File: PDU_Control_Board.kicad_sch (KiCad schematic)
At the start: 203 parts, among them J1 Current_Sensor, J10 Precharge_2, J11 Shunt_2, J12 VIN_Enable, J13 1-776087-1, J2 Shunt_1, J20 VDC_OUT2, J21 VDC_OUT1, J22 VDC_IN, J3 SWD, J4 Precharge_1, J5 Precharge_2, J6 Shunt_2, J7 VIN_Enable, J8 Precharge_1, J9 Shunt_1, Q1 BSP75N, Q10 BC817, Q2 BSP75N, Q3 BSP75N, Q4 BSP75N, Q5 BSP75N, Q6 BC817, Q7 BC817, Q8 BC817, Q9 BC817, U1 LMV321, U2 APM32F405xG, U3 LMV321, U4 LMV321, U5 LMV321, U6 LMV321, Y2 X322516MOB4SI

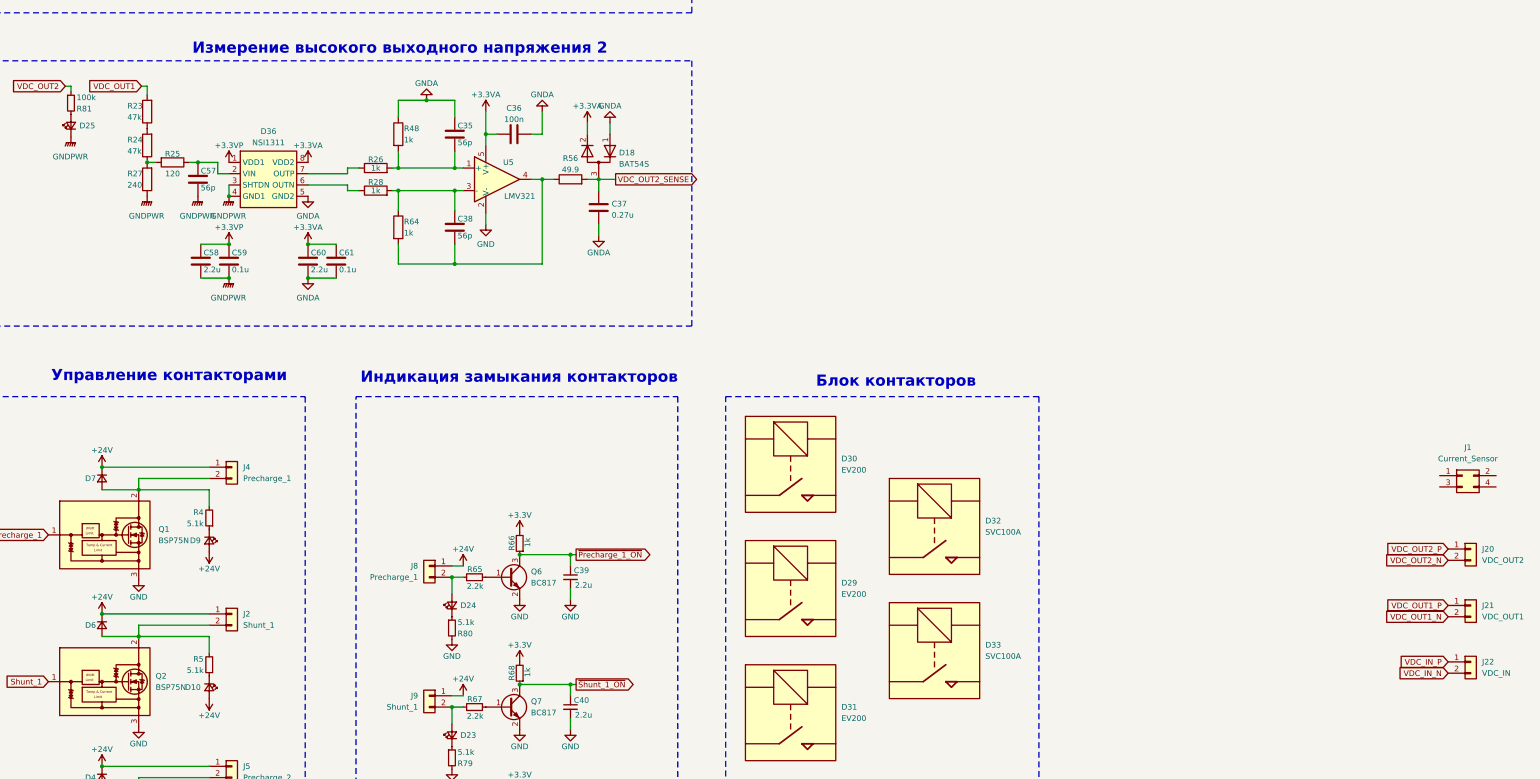
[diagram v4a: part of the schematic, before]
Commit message: VER1.0: обрезал плату
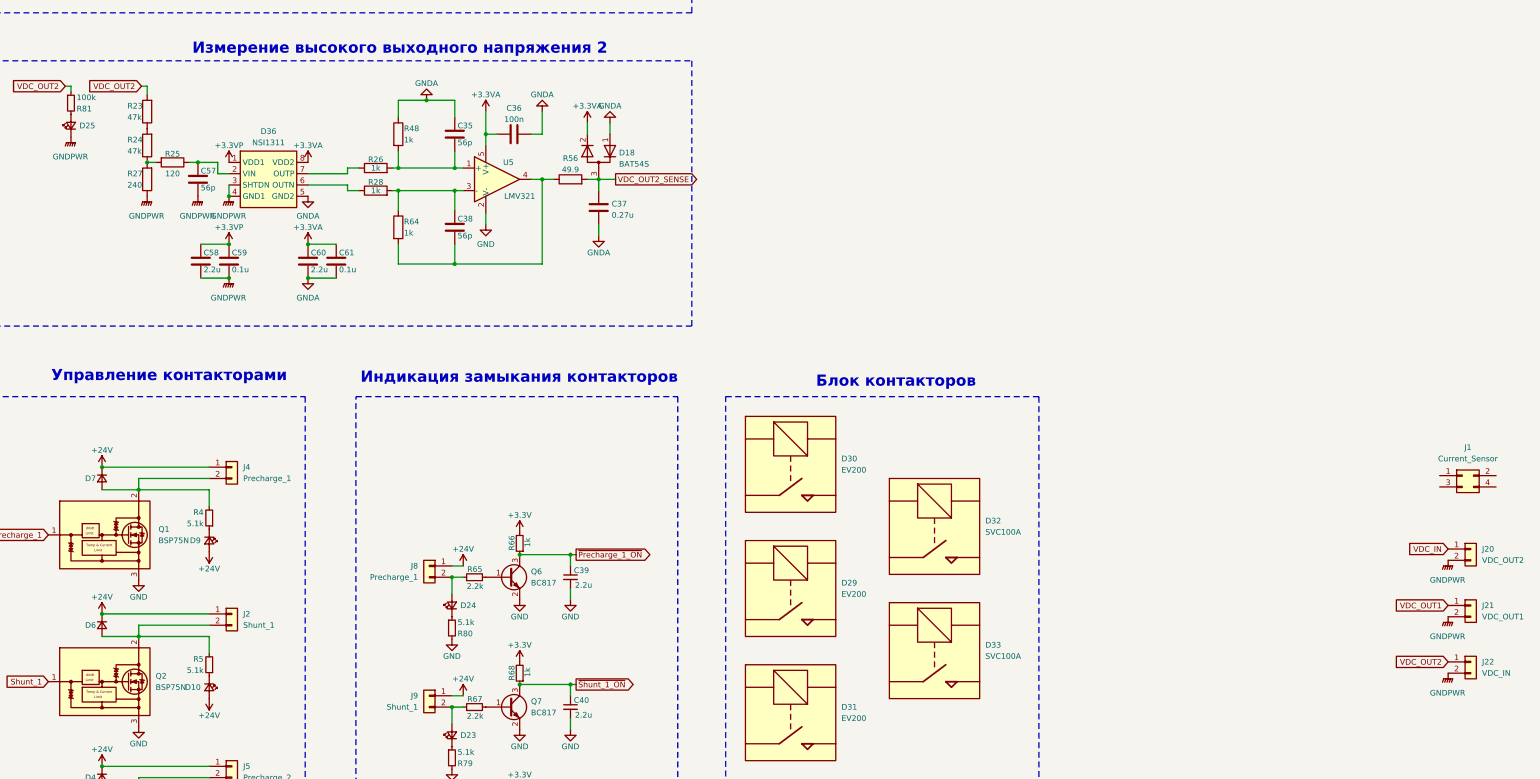
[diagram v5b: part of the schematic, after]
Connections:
- net VDC_IN_N is gone; now on net GNDPWR: J22.2 (Pin_2)
- net VDC_IN_P is gone; now on net VDC_OUT2: J22.1 (Pin_1)
- net VDC_OUT1_N is gone; now on net GNDPWR: J21.2 (Pin_2)
- net VDC_OUT2_N is gone; now on net GNDPWR: J20.2 (Pin_2)
- net VDC_OUT2_P is gone; now on net VDC_IN: J20.1 (Pin_1)
- net VDC_OUT1: now also J21.1 (Pin_1); no longer R23.2
- net VDC_OUT1_P: no longer J21.1 (Pin_1)
- net VDC_OUT2: now also R23.2
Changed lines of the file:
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@@
 		)
 	)
-	(global_label "VDC_OUT1_P"
+	(global_label "VDC_IN"
 		(shape input)
-		(at 946.15 527.05 180)
+		(at 946.15 514.35 180)
 		(fields_autoplaced yes)
 		(effects
@@
 		)
 		(property "Intersheetrefs" "${INTERSHEET_REFS}"
-			(at 933.3433 527.05 0)
+			(at 937.7939 514.35 0)
 			(effects
 				(font
@@
 		)
 	)
-	(global_label "~{Precharge_1_ON}"
+	(global_label "VDC_OUT1"
 		(shape input)
-		(at 307.34 323.85 0)
+		(at 946.15 527.05 180)
 		(fields_autoplaced yes)
 		(effects
@@
 				(size 1.27 1.27)
 			)
-			(justify left)
+			(justify right)
 		)
 		(property "Intersheetrefs" "${INTERSHEET_REFS}"
-			(at 325.6861 323.85 0)
+			(at 935.5047 527.05 0)
 			(effects
 				(font
 					(size 1.27 1.27)
 				)
-				(justify left)
+				(justify right)
 				(hide yes)
 			)
 		)
 	)
-	(global_label "VDC_IN_SENSE"
+	(global_label "~{Precharge_1_ON}"
 		(shape input)
-		(at 307.34 400.05 0)
+		(at 307.34 323.85 0)
 		(fields_autoplaced yes)
 		(effects
@@
 		)
 		(property "Intersheetrefs" "${INTERSHEET_REFS}"
-			(at 323.8718 400.05 0)
+			(at 325.6861 323.85 0)
 			(effects
 				(font
@@
 		)
 	)
-	(global_label "Current"
+	(global_label "VDC_IN_SENSE"
 		(shape input)
-		(at 797.56 295.91 180)
+		(at 307.34 400.05 0)
 		(fields_autoplaced yes)
 		(effects
@@
 				(size 1.27 1.27)
 			)
-			(justify right)
+			(justify left)
 		)
 		(property "Intersheetrefs" "${INTERSHEET_REFS}"
-			(at 787.6201 295.91 0)
+			(at 323.8718 400.05 0)
 			(effects
 				(font
 					(size 1.27 1.27)
 				)
-				(justify right)
+				(justify left)
 				(hide yes)
 			)
 		)
 	)
-	(global_label "VDC_OUT2_P"
+	(global_label "Current"
 		(shape input)
-		(at 946.15 514.35 180)
+		(at 797.56 295.91 180)
 		(fields_autoplaced yes)
 		(effects
@@
 		)
 		(property "Intersheetrefs" "${INTERSHEET_REFS}"
-			(at 933.089 514.35 0)
+			(at 787.6201 295.91 0)
 			(effects
 				(font
@@
 		)
 	)
-	(global_label "VDC_OUT1_N"
-		(shape input)
-		(at 946.15 529.59 180)
-		(fields_autoplaced yes)
-		(effects
-			(font
-				(size 1.27 1.27)
-			)
-			(justify right)
-		)
-		(property "Intersheetrefs" "${INTERSHEET_REFS}"
-			(at 933.3433 529.59 0)
-			(effects
-				(font
-					(size 1.27 1.27)
-				)
-				(justify right)
-				(hide yes)
-			)
-		)
-	)
 	(global_label "Shunt_1"
 		(shape input)
@@
 		)
 	)
-	(global_label "VDC_IN_P"
-		(shape input)
-		(at 946.15 539.75 180)
-		(fields_autoplaced yes)
-		(effects
-			(font
-				(size 1.27 1.27)
-			)
-			(justify right)
-		)
-		(property "Intersheetrefs" "${INTERSHEET_REFS}"
-			(at 935.6325 539.75 0)
-			(effects
-				(font
-					(size 1.27 1.27)
-				)
-				(justify right)
-				(hide yes)
-			)
-		)
-	)
-	(global_label "VDC_OUT1"
+	(global_label "VDC_OUT2"
 		(shape input)
 		(at 652.145 410.21 180)
@@
 		)
 		(property "Intersheetrefs" "${INTERSHEET_REFS}"
-			(at 641.4997 410.21 0)
+			(at 639.7255 410.21 0)
 			(effects
 				(font
@@
 		)
 	)
-	(global_label "CAN1_RXD_MCU"
-		(shape bidirectional)
-		(at 307.34 331.47 0)
+	(global_label "VDC_OUT2"
+		(shape input)
+		(at 946.15 539.75 180)
 		(fields_autoplaced yes)
 		(effects
@@
 				(size 1.27 1.27)
 			)
-			(justify left)
+			(justify right)
 		)
 		(property "Intersheetrefs" "${INTERSHEET_REFS}"
-			(at 325.9923 331.47 0)
+			(at 933.7305 539.75 0)
 			(effects
 				(font
 					(size 1.27 1.27)
 				)
-				(justify left)
+				(justify right)
 				(hide yes)
 			)
 		)
 	)
-	(global_label "VDC_IN_N"
-		(shape input)
-		(at 946.15 542.29 180)
+	(global_label "CAN1_RXD_MCU"
+		(shape bidirectional)
+		(at 307.34 331.47 0)
 		(fields_autoplaced yes)
 		(effects
@@
 				(size 1.27 1.27)
 			)
-			(justify right)
+			(justify left)
 		)
 		(property "Intersheetrefs" "${INTERSHEET_REFS}"
-			(at 935.6325 542.29 0)
+			(at 325.9923 331.47 0)
 			(effects
 				(font
 					(size 1.27 1.27)
 				)
-				(justify right)
+				(justify left)
 				(hide yes)
 			)
@@
 		)
 	)
-	(global_label "VDC_OUT2_N"
-		(shape input)
-		(at 946.15 516.89 180)
-		(fields_autoplaced yes)
-		(effects
-			(font
-				(size 1.27 1.27)
-			)
-			(justify right)
-		)
-		(property "Intersheetrefs" "${INTERSHEET_REFS}"
-			(at 933.089 516.89 0)
-			(effects
-				(font
-					(size 1.27 1.27)
-				)
-				(justify right)
-				(hide yes)
-			)
-		)
-	)
 	(symbol
 		(lib_id "power:GNDA")
@@
 	)
 	(symbol
+		(lib_id "power:GNDPWR")
+		(at 946.15 529.59 0)
+		(unit 1)
+		(exclude_from_sim no)
+		(in_bom yes)
+		(on_board yes)
+		(dnp no)
+		(fields_autoplaced yes)
+		(property "Reference" "#PWR0160"
+			(at 946.15 534.67 0)
+			(effects
+				(font
+					(size 1.27 1.27)
+				)
+				(hide yes)
+			)
+		)
+		(property "Value" "GNDPWR"
+			(at 946.023 534.035 0)
+			(effects
+				(font
+					(size 1.27 1.27)
+				)
+			)
+		)
+		(property "Footprint" ""
+			(at 946.15 530.86 0)
+			(effects
+				(font
+					(size 1.27 1.27)
+				)
+				(hide yes)
+			)
+		)
+		(property "Datasheet" ""
+			(at 946.15 530.86 0)
+			(effects
+				(font
+					(size 1.27 1.27)
+				)
+				(hide yes)
+			)
+		)
+		(property "Description" "Power symbol creates a global label with name \"GNDPWR\" , global ground"
+			(at 946.15 529.59 0)
+			(effects
+				(font
+					(size 1.27 1.27)
+				)
+				(hide yes)
+			)
+		)
+		(pin "1"
+		)
+		(instances
+			(project "PDU_Control_Board"
+				(path "/7b040528-7065-4d6b-8722-075d9f593d01"
+					(reference "#PWR0160")
+					(unit 1)
+				)
+			)
+		)
+	)
+	(symbol
 		(lib_id "Connector_Generic:Conn_01x02")
 		(at 672.465 596.265 0)
@@
 	)
 	(symbol
+		(lib_id "power:GNDPWR")
+		(at 946.15 542.29 0)
+		(unit 1)
+		(exclude_from_sim no)
+		(in_bom yes)
+		(on_board yes)
+		(dnp no)
+		(fields_autoplaced yes)
+		(property "Reference" "#PWR0159"
+			(at 946.15 547.37 0)
+			(effects
+				(font
+					(size 1.27 1.27)
+				)
+				(hide yes)
+			)
+		)
+		(property "Value" "GNDPWR"
+			(at 946.023 546.735 0)
+			(effects
+				(font
+					(size 1.27 1.27)
+				)
+			)
+		)
+		(property "Footprint" ""
+			(at 946.15 543.56 0)
+			(effects
+				(font
+					(size 1.27 1.27)
+				)
+				(hide yes)
+			)
+		)
+		(property "Datasheet" ""
+			(at 946.15 543.56 0)
+			(effects
+				(font
+					(size 1.27 1.27)
+				)
+				(hide yes)
+			)
+		)
+		(property "Description" "Power symbol creates a global label with name \"GNDPWR\" , global ground"
+			(at 946.15 542.29 0)
+			(effects
+				(font
+					(size 1.27 1.27)
+				)
+				(hide yes)
+			)
+		)
+		(pin "1"
+		)
+		(instances
+			(project "PDU_Control_Board"
+				(path "/7b040528-7065-4d6b-8722-075d9f593d01"
+					(reference "#PWR0159")
+					(unit 1)
+				)
+			)
+		)
+	)
+	(symbol
 		(lib_id "Device:R_Small")
 		(at 252.73 298.45 0)
@@
 					(unit 1)
 				)
+			)
+		)
+	)
+	(symbol
+		(lib_id "power:GNDPWR")
+		(at 946.15 516.89 0)
+		(unit 1)
+		(exclude_from_sim no)
+		(in_bom yes)
+		(on_board yes)
+		(dnp no)
+		(fields_autoplaced yes)
+		(property "Reference" "#PWR0161"
+			(at 946.15 521.97 0)
+			(effects
+				(font
+					(size 1.27 1.27)
+				)
+				(hide yes)
+			)
+		)
+		(property "Value" "GNDPWR"
+			(at 946.023 521.335 0)
+			(effects
+				(font
+					(size 1.27 1.27)
+				)
+			)
+		)
+		(property "Footprint" ""
+			(at 946.15 518.16 0)
+			(effects
+				(font
+					(size 1.27 1.27)
+				)
+				(hide yes)
+			)
+		)
+		(property "Datasheet" ""
+			(at 946.15 518.16 0)
+			(effects
+				(font
+					(size 1.27 1.27)
+				)
+				(hide yes)
+			)
+		)
+		(property "Description" "Power symbol creates a global label with name \"GNDPWR\" , global ground"
+			(at 946.15 516.89 0)
+			(effects
+				(font
+					(size 1.27 1.27)
+				)
+				(hide yes)
+			)
+		)
+		(pin "1"
+		)
+		(instances
+			(project "PDU_Control_Board"
+				(path "/7b040528-7065-4d6b-8722-075d9f593d01"
+					(reference "#PWR0161")
+					(unit 1)
+				)

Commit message: VER1.0: разместил все компоненты на плате
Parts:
- removed R32, R40: 249k, Resistor_SMD:R_1206_3216Metric, symbol Device:R
- added C65: 10u, Capacitor_Tantalum_SMD:CP_EIA-3528-21_Kemet-B_Pad1.50x2.35mm_HandSolder, symbol Device:C_Polarized
- added H1: MountingHole_Pad, MountingHole:MountingHole_3.2mm_M3_Pad_Via, symbol Mechanical:MountingHole_Pad
- added J14: Resistor, Connector_Molex:Molex_Mini-Fit_Jr_5566-06A_2x03_P4.20mm_Vertical, symbol Connector_Generic:Conn_02x03_Top_Bottom
- added J15: GNDPWR, Connector_My:Mini-Fit_01x02_Vertical, symbol Connector_Generic:Conn_01x02
- added J16: VDC_OUT1_Relay, Connector_My:Mini-Fit_01x02_Vertical, symbol Connector_Generic:Conn_01x02
- added J17: VDC_OUT2_Rela, Connector_My:Mini-Fit_01x02_Vertical, symbol Connector_Generic:Conn_01x02
- C62: footprint (none) -> Capacitor_Tantalum_SMD:CP_EIA-6032-28_Kemet-C_Pad2.25x2.35mm_HandSolder
- C63: footprint (none) -> Capacitor_Tantalum_SMD:CP_EIA-7360-38_Kemet-E_Pad2.25x4.25mm_HandSolder
- C64: footprint (none) -> Capacitor_Tantalum_SMD:CP_EIA-3528-21_Kemet-B_Pad1.50x2.35mm_HandSolder
- J20: value VDC_OUT2 -> VDC_IN
- J22: value VDC_IN -> VDC_OUT2
- L1: value L -> 4.7u; footprint (none) -> Inductor_SMD:L_1812_4532Metric_Pad1.30x3.40mm_HandSolder
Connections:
- net +3.3VP: now also C64.1, D37.6 (+Vo)
- net GND: now also H1.1; no longer U5.2 (V-)
- net GNDA: now also U5.2 (V-)
- net GNDPWR: now also C64.2, D37.7 (0V), C65.2, J15.1 (Pin_1), J15.2 (Pin_2); no longer J20.2 (Pin_2), J21.2 (Pin_2), J22.2 (Pin_2)
- net VDC_IN: now also J20.2 (Pin_2), J14.3 (Pin_3), J14.6 (Pin_6)
- net VDC_OUT1: now also J21.2 (Pin_2)
- net VDC_OUT2: now also J22.2 (Pin_2)
- net at D37.8 (CS): now also C65.1
- new net VDC_OUT1_Relay: J14.1 (Pin_1), J14.4 (Pin_4), J16.1 (Pin_1), J16.2 (Pin_2)
- new net VDC_OUT2_Relay: J14.2 (Pin_2), J14.5 (Pin_5), J17.1 (Pin_1), J17.2 (Pin_2)
- no-connect marks 49 -> 48
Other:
- moved on the sheet: C64

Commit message: VER1.0: трассировал все дорожки и полигоны
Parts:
- removed C1: 4.7u, Capacitor_SMD:C_0805_2012Metric_Pad1.18x1.45mm_HandSolder, symbol Device:C_Small
- removed C2: 100n, Capacitor_SMD:C_0805_2012Metric_Pad1.18x1.45mm_HandSolder, symbol Device:C_Small
- removed C3: 1u, Capacitor_SMD:C_0805_2012Metric_Pad1.18x1.45mm_HandSolder, symbol Device:C_Small
- removed FB1: BLM21BD121SN1D, Inductor_SMD:L_0805_2012Metric_Pad1.15x1.40mm_HandSolder, symbol Device:FerriteBead_Small
- removed R1: 0, Resistor_SMD:R_0805_2012Metric_Pad1.20x1.40mm_HandSolder, symbol Device:R_Small
- added C66: 22u, Capacitor_Tantalum_SMD:CP_EIA-7343-43_Kemet-X_Pad2.25x2.55mm_HandSolder, symbol Device:C_Polarized_Small
- added C67: 2.2n, Capacitor_SMD:C_0805_2012Metric_Pad1.18x1.45mm_HandSolder, symbol Device:C
- added C68: 47n, Capacitor_SMD:C_0805_2012Metric_Pad1.18x1.45mm_HandSolder, symbol Device:C
- added C69: 10u, Capacitor_SMD:C_1210_3225Metric_Pad1.33x2.70mm_HandSolder, symbol Device:C_Small
- added C70: 330u, Capacitor_Tantalum_SMD:CP_EIA-6032-28_Kemet-C_Pad2.25x2.35mm_HandSolder, symbol Device:C_Polarized_Small
- added C71: 22u, Capacitor_SMD:C_1210_3225Metric_Pad1.33x2.70mm_HandSolder, symbol Device:C_Small
- added D40, D42: LED_Small, LED_SMD:LED_0805_2012Metric, symbol Device:LED_Small
- added D41: K7805-1000R3, MORNSUN:K78xx-1000R3, symbol MORNSUN:K78xx-1000R3
- added H2, H3, H6: MountingHole_Pad, MountingHole:MountingHole_4.3mm_M4, symbol Mechanical:MountingHole_Pad
- added H4: MountingHole_Pad, MountingHole:MountingHole_4.3mm_M4_Pad_Via, symbol Mechanical:MountingHole_Pad
- added R32: 665, Resistor_SMD:R_0805_2012Metric_Pad1.20x1.40mm_HandSolder, symbol Device:R
- added R35: DNP, Resistor_SMD:R_0805_2012Metric_Pad1.20x1.40mm_HandSolder, symbol Device:R
- added R36: 1k, Resistor_SMD:R_0805_2012Metric_Pad1.20x1.40mm_HandSolder, symbol Device:R
- added R37: 750, Resistor_SMD:R_0805_2012Metric_Pad1.20x1.40mm_HandSolder, symbol Device:R_Small
- added R38: 1.1k, Resistor_SMD:R_0805_2012Metric_Pad1.20x1.40mm_HandSolder, symbol Device:R_Small
- H1: footprint MountingHole:MountingHole_3.2mm_M3_Pad_Via -> MountingHole:MountingHole_4.3mm_M4_Pad_Via
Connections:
- net +3.3VA is gone; now on net +3.3V: C21.1, C22.1, C31.1, C36.1, C44.1, C50.2, C51.1, C55.2, C56.1, C60.2, C61.1, D17.2 (K), D18.2 (K), D28.2 (K), D34.8 (VDD2), D35.8 (VDD2), D36.8 (VDD2), D5.2 (K), U1.5 (V+), U2.21 (VREF+), U2.22 (VDDA), U3.5 (V+), U4.5 (V+), U5.5 (V+), U6.5 (V+)
- net CAN1H is gone; now on net CANH: C17.2, D1.7 (CANH), D2.1 (K), R6.2
- net CAN1L is gone; now on net CANL: C20.1, D1.6 (CANL), D2.2 (K), R6.1
- net GNDA is gone; now on net GND: C21.2, C22.2, C23.2, C27.2, C28.2, C30.1, C31.2, C32.2, C35.1, C36.2, C37.2, C44.2, C45.2, C46.2, C50.1, C51.2, C55.1, C56.2, C60.1, C61.2, C8.1, D17.1 (K), D18.1 (K), D28.1 (K), D34.5 (GND2), D35.5 (GND2), D36.5 (GND2), D5.1 (K), R14.1, R31.1, R48.1, R9.2, U1.2 (V-), U2.20 (VSSA), U3.2 (V-), U4.2 (V-), U5.2 (V-), U6.2 (V-)
- net +24V: now also J13.1, C66.1, C69.2, D41.1 (Vin)
- net +3.3VP: now also D40.2 (A)
- net Current_SENSE: now also U2.33 (PC4); no longer U2.30 (PA5)
- net GND: now also J1.2 (Pin_2), J1.4 (Pin_4), J13.16, R33.2, R34.2, C66.2, C67.2, C68.2, C69.1, C70.2, C71.2, D41.2 (GND(-Vo)), H4.1, R36.2, R38.2; no longer D38.1 (K), D39.1 (K)
- net GNDPWR: now also R37.2
- net Precharge_1: now also U2.68 (PA9); no longer U2.66 (PC9)
- net Precharge_2: now also U2.66 (PC9); no longer U2.62 (PD15)
- net Shunt_1: now also U2.62 (PD15); no longer U2.64 (PC7)
- net Shunt_2: now also U2.64 (PC7); no longer U2.60 (PD13)
- net VDC_IN_SENSE: now also U2.32 (PA7); no longer U2.33 (PC4)
- net VDC_OUT1_SENSE: now also U2.31 (PA6); no longer U2.32 (PA7)
- net VDC_OUT2_SENSE: now also U2.30 (PA5); no longer U2.31 (PA6)
- net VIN_Enable: no longer U2.68 (PA9)
- net ~{Precharge_1_ON}: now also U2.69 (PA10); no longer U2.67 (PA8)
- net ~{Precharge_2_ON}: now also U2.67 (PA8); no longer U2.63 (PC6)
- net ~{Shunt_1_ON}: now also U2.63 (PC6); no longer U2.65 (PC8)
- net ~{Shunt_2_ON}: now also U2.65 (PC8); no longer U2.61 (PD14)
- net ~{VIN_Enable_ON}: now also U2.98 (PE1); no longer U2.69 (PA10)
- net at D38.2 (A): now also U2.52 (PB13); no longer R33.2
- net at R34.1: now also D39.1 (K); no longer U2.40 (PE9)
- net at D39.2 (A): now also U2.57 (PD10); no longer R34.2
- net at R33.1: now also D38.1 (K); no longer U2.39 (PE8)
- net CANL: now reaches J13.2
- net CANH: now reaches J13.3
- net Crrent_Out: now reaches J1.1 (Pin_1)
- net Crrent_Out: now also C67.1, R32.2, R35.1
- net +5V: now reaches J1.3 (Pin_3)
- net +5V: now also C68.1, C70.1, C71.1, D41.3 (+Vo(GND)), D42.2 (A), R35.2
- net Current: no longer names the net of R85.1
- net Current: now also R32.1, R36.1
- new net: D42.1 (K), R38.1
- new net: D40.1 (K), R37.1
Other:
- note added: "Питание 3.3В отвязанные"
- note added: "Питание 5В"
- moved on the sheet: C44, C45, C46, C62, C63, C64, C65, D28, D37, D38, D39, L1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

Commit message: VER2.0: добавил зарядные резисторы
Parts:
- removed J14: Resistor, Connector_Molex:Molex_Mini-Fit_Jr_5566-06A_2x03_P4.20mm_Vertical, symbol Connector_Generic:Conn_02x03_Top_Bottom
- added R1, R40, R41, R42, R43, R44, R45, R46, R49, R50, R51, R52, R53, R54, R55, R57: 10k, Resistor_THT:R_Axial_Power_L60.0mm_W14.0mm_P66.04mm, symbol Device:R
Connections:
- net VDC_IN: now also R1.1, R40.1, R41.1, R42.1, R43.1, R44.1, R45.1, R46.1, R49.1, R50.1, R51.1, R52.1, R53.1, R54.1, R55.1, R57.1
- net VDC_OUT1_Relay: now also R1.2, R40.2, R41.2, R42.2, R43.2, R44.2, R45.2, R46.2
- net VDC_OUT2_Relay: now also R49.2, R50.2, R51.2, R52.2, R53.2, R54.2, R55.2, R57.2
